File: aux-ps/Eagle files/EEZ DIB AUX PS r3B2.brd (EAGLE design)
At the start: 230.5 x 60 mm, 86 parts, among them IC2 MAX31760AEE+, IC3 BD00FC0WFP, J1 PF0030/PC, J2 4907, J3 4907, J4 4907, J5 SWEB 8094 AU/GN, Q1 BTA26-600, Q2 BTA26-600, Q3 2N7002, Q4 2N7002, Q5 2N7002, SW1 DF62J12S2AHQA, SW2 OS102011MA1QN1C, X1 39-28-1063, X2 39-30-1039, X3 ZL231-16PG, X4 47053-1000, X5 47053-1000

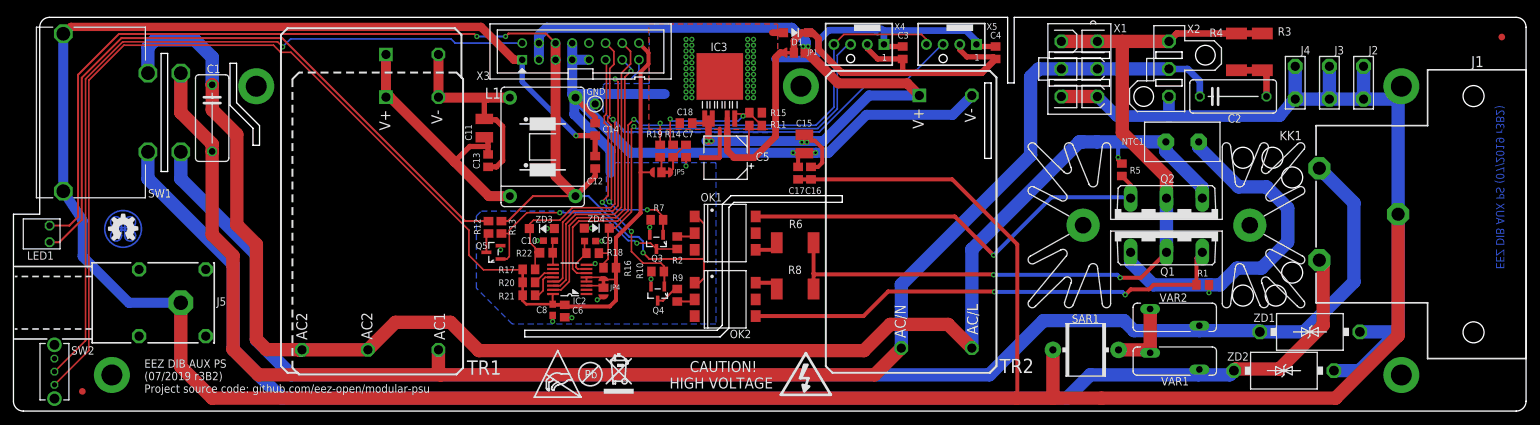
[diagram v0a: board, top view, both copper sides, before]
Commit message: AUX-PS PCB redesign
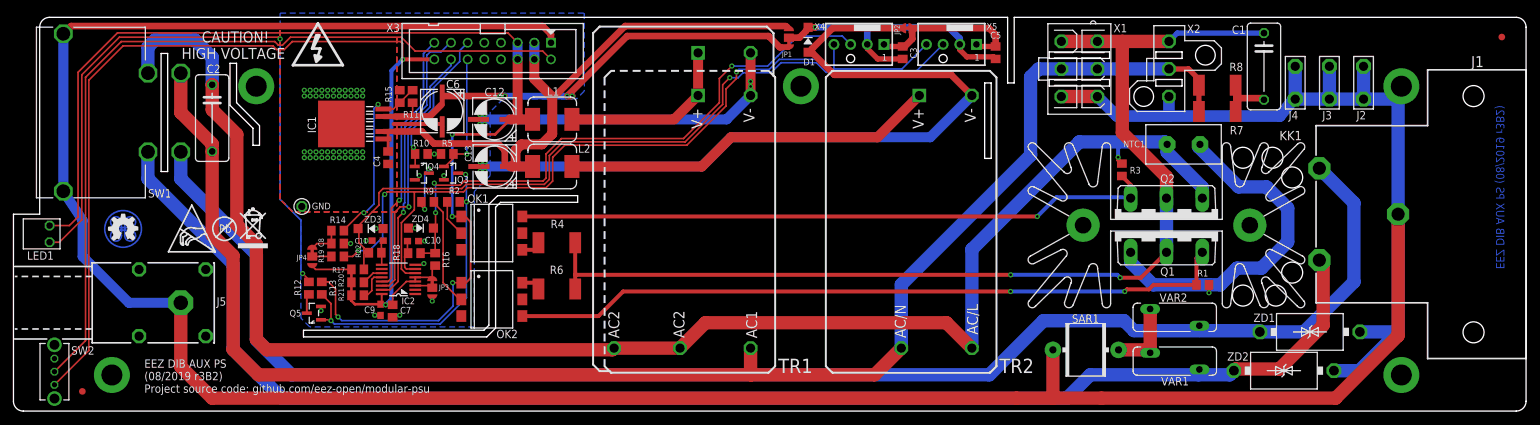
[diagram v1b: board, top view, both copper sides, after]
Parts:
- removed C14, C16, C17: (no value), rcl:C0805
- removed C15: 4u7, rcl:C1210
- removed C18: N.C., rcl:C0805
- removed IC3: BD00FC0WFP, EEZ_DIB:KVU5
- removed JP5: JP3-CUT, EEZ_Lib1:JP3-CUT
- added IC1: BD00FC0WFP, EEZ_DIB:KVU5
- added JP2: JP2-NOCUT, EEZ_Lib1:JP2-NOCUT
- added L2: VLS6045AF-3R3N, EEZ_inductors_and_transformers:COILCRAFT_HPI0630
- C11: value 4u7 -> 100n; device rcl:C1210 -> rcl:C0603
- C12, C13: value (none) -> EEEFK1V470P; device rcl:C0805 -> EEZ_Lib1:CAPAE660X610N
- C4: value 1u -> N.C.
- C5: value EEEFK1V470P -> 1u; device EEZ_Lib1:CAPAE660X610N -> rcl:C0805
- C6: value 1u -> EEEFK1V470P; device rcl:C0805 -> EEZ_Lib1:CAPAE660X610N
- C8: value 100n -> 1u; device rcl:C0603 -> rcl:C0805
- JP3: value JP2-NOCUT -> JP3-CUT; device EEZ_Lib1:JP2-NOCUT -> EEZ_Lib1:JP3-CUT
- L1: value (none) -> VLS6045AF-3R3N; device EEZ_inductors_and_transformers:RN212 -> EEZ_inductors_and_transformers:COILCRAFT_HPI0630
- R3: value 330R/2W -> 2K2; device rcl:R2512 -> rcl:R0805
- R5: value 2K2 -> 47K
- R7: value 47K -> 330R/2W; device rcl:R0805 -> rcl:R2512
- X3: value ZL231-16PG -> DS1013-16SSIB1
- moved C1 160.5 mm to (190.6, 52.5)
- moved C2 155.6 mm to (30.3, 44.6), turned to 270 degrees
- moved R4 107.6 mm to (82.8, 25.7), turned to 0 degrees
- moved R5 102.8 mm to (66.1, 39.2), turned to 0 degrees
- moved C4 94.0 mm to (57.1, 38.6), turned to 270 degrees
- moved R7 87.0 mm to (183.5, 45.7)
- moved JP3 78.7 mm to (63.8, 18.8), flipped to the top, turned to 270 degrees
- moved R8 71.4 mm to (183.5, 49.7)
- moved U$2 60.0 mm to (32.2, 27.8)
- moved U$3 60.0 mm to (34.2, 24.8)
- moved U$4 60.0 mm to (23.6, 24.3)
- moved R15 54.3 mm to (58.9, 47.9), turned to 90 degrees
- moved R14 52.5 mm to (49.4, 27.5), turned to 180 degrees
- moved R11 52.4 mm to (60.8, 47.9), turned to 90 degrees
- moved R19 51.7 mm to (49.4, 23.6), turned to 0 degrees
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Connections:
- removed net N$27: C11.1, C13.2, L1.1, TR1.V+, TR1.V+1
- removed net N$28: C11.2, C13.1, L1.3, TR1.V-, TR1.V-1
- new net N$15: L1.1, TR1.V+, TR1.V+1
- new net N$8: L2.1, TR2.V+
- net +12V: now also C13.1, C4.1, IC1.1, IC1.2, L2.2; no longer C15.1, C16.2, C18.1, IC3.1, IC3.2, TR2.V+
- net +3V3: now also C7.2, C9.2, JP3.NC, JP4.NO; no longer C6.2, C8.2, JP4.NC, JP5.NO
- net +5V: now also C12.1; no longer C12.2
- net 12V_PWM: now also C6.1, IC1.4; no longer C5.1, IC3.4
- net AC_L_OUT: now also C2.1, R3.2; no longer C1.1, R5.2
- net AC_N_OUT: now also C2.2, R7.1, R8.1; no longer C1.2, C2.1
- net AC_OUT_L: now also C1.1, R4.2; no longer R3.1, R4.1, R8.2
- net FAN_OUT+: now also C5.1; no longer C4.1
- net FAN_OUT-: now also C5.2, JP2.2; no longer C4.2, JP3.2
- net GND: now also C11.2, C12.2, C13.2, C4.2, C6.2, C7.1, C8.2, C9.1, IC1.3, JP2.1, JP3.NO, R5.1, TR1.V-, TR1.V-1; no longer C14.1, C15.2, C17.1, C18.2, C5.2, C6.1, C7.2, C8.1, C9.2, IC3.3, JP3.1, JP4.NO, L1.4, R7.1
- net N$11: now also IC1.5; no longer IC3.5
- net N$2: now also C10.1; no longer C9.1
- net N$21: now also C11.1; no longer C10.1
- net N$23: now also JP3.COM; no longer JP4.COM
- net N$4: now also JP4.COM; no longer JP5.COM
- net N$71: now also R3.1; no longer R5.1
- net N$73: now also R6.1; no longer R8.1
- net N$76: now also R4.1; no longer R6.1
- net N$83: now also C1.2, R7.2, R8.2; no longer C2.2, R3.2, R4.2
- net N$9: now also C8.1, JP4.NC; no longer C7.1, JP5.NC
- net PE: no longer C12.1, C14.2, C16.1, C17.2
- net PWR_DIRECT: now also R5.2; no longer R7.2
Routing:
- net PE: track 561.8 -> 484.2 mm, vias 3 -> 2
- net N$8: track 0.00 -> 57.4 mm
- net N$27: track 40.8 -> 0.00 mm
- net 12V_PWM: track 33.5 -> 73.0 mm, vias 0 -> 4
- net AC_OUT_L: track 128.7 -> 165.3 mm
- net PWM_OUT: track 93.5 -> 129.9 mm, vias 2 -> 3
- net GND: track 160.9 -> 196.2 mm, vias 58 -> 67
- net N$72: track 74.9 -> 110.0 mm
- net N$28: track 32.0 -> 0.00 mm
- net N$71: track 67.3 -> 98.0 mm
- net +12V: track 124.0 -> 95.0 mm, vias 6 -> 0
- net +3V3: track 204.7 -> 177.1 mm, vias 0 -> 2
- net N$15: track 0.00 -> 27.2 mm
- net FAN_SENSE1: track 68.7 -> 91.7 mm, vias 1 -> 3
- net FAN_SENSE2: track 92.0 -> 114.6 mm
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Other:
- outline, holes or cut-outs redrawn
- board text added: "EEZ DIB AUX PS (08/2019 r3B2)"
- board text added: "EEZ DIB AUX PS (08/2019 r3B2) Project source code: github.com/eez-open/modular-psu"
- board text removed: "EEZ DIB AUX PS (07/2019 r3B2)"
- board text removed: "EEZ DIB AUX PS (07/2019 r3B2) Project source code: github.com/eez-open/modular-psu"

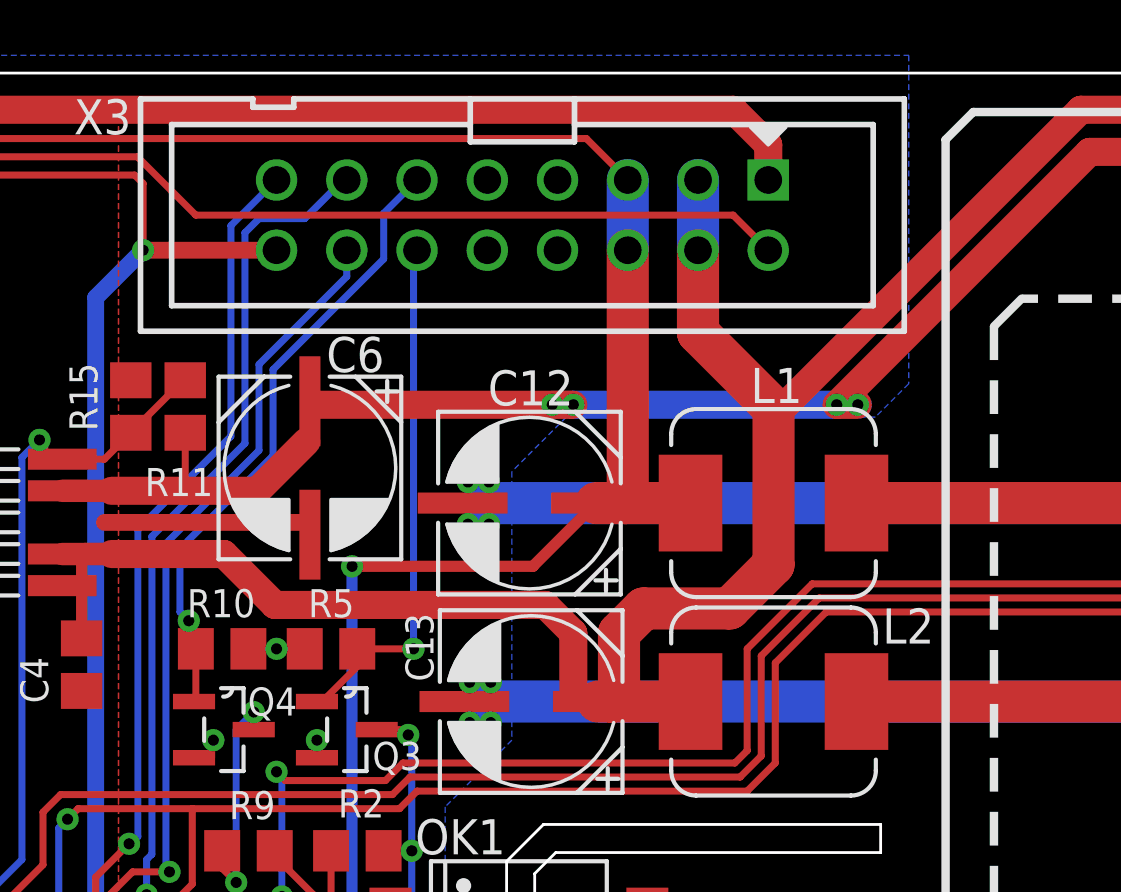
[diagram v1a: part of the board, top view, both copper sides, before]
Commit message: PCB test tabs added
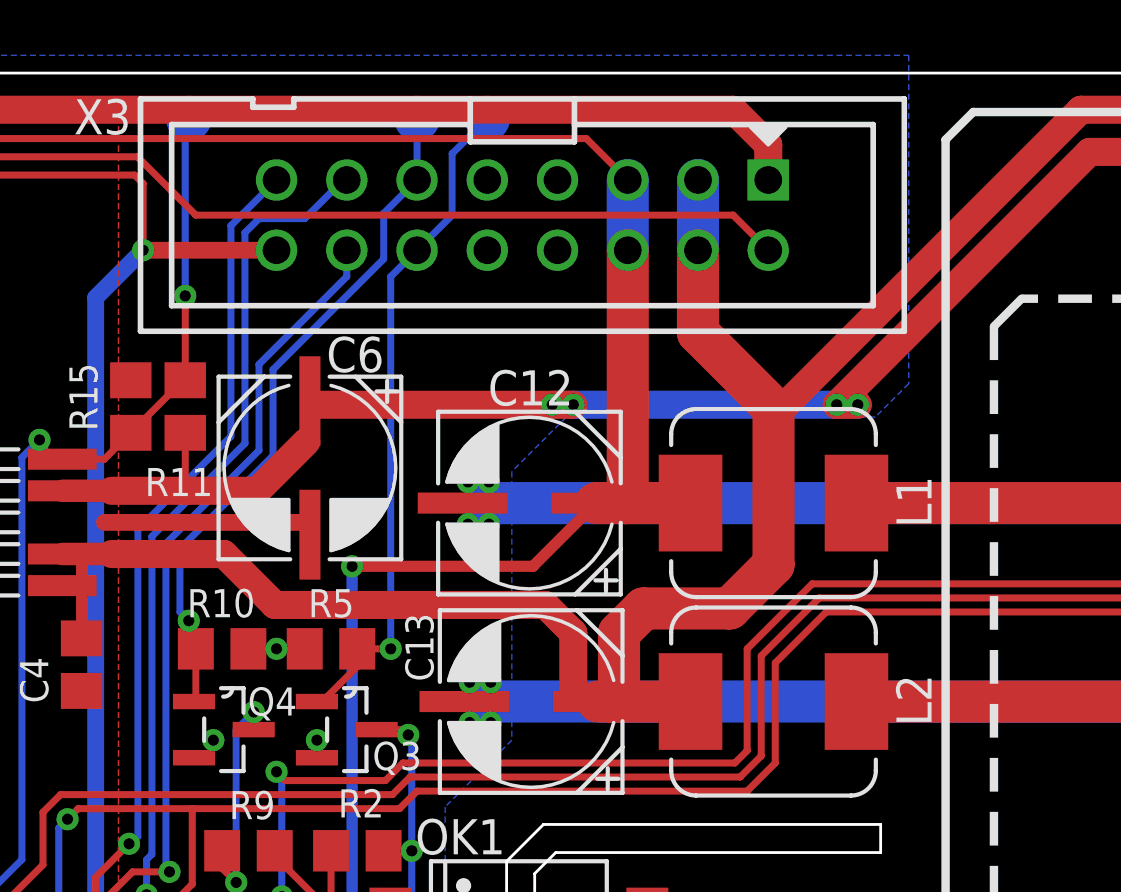
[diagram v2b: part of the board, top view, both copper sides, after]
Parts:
- added DIR, FB, SS: (no value), EEZ_Lib1:PCB_TEST_PAD
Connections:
- removed net N$11: IC1.5, R11.2, R14.1, R15.1
- new net LDO_FB: FB.NC, IC1.5, R11.2, R14.1, R15.1
- net PWR_DIRECT: now also DIR.NC
- net PWR_SSTART: now also SS.NC
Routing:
- net LDO_FB: track 0.00 -> 38.6 mm, vias 0 -> 3
- net N$11: track 29.1 -> 0.00 mm, vias 2 -> 0
- net PWR_DIRECT: track 19.3 -> 24.5 mm
- net PWR_SSTART: track 23.4 -> 25.7 mm
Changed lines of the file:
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@@
 <grid distance="2.5" unitdist="mil" unit="mil" style="lines" multiple="40" display="no" altdistance="12.5" altunitdist="mil" altunit="mil"/>
 <layers>
-<layer number="1" name="Top" color="11" fill="1" visible="no" active="yes"/>
+<layer number="1" name="Top" color="11" fill="1" visible="yes" active="yes"/>
 <layer number="2" name="Route2" color="1" fill="3" visible="no" active="no"/>
 <layer number="3" name="Route3" color="4" fill="3" visible="no" active="no"/>
@@
 <layer number="14" name="Route14" color="1" fill="6" visible="no" active="no"/>
 <layer number="15" name="Route15" color="4" fill="6" visible="no" active="no"/>
-<layer number="16" name="Bottom" color="1" fill="1" visible="no" active="yes"/>
-<layer number="17" name="Pads" color="6" fill="1" visible="no" active="yes"/>
-<layer number="18" name="Vias" color="6" fill="1" visible="no" active="yes"/>
-<layer number="19" name="Unrouted" color="6" fill="1" visible="no" active="yes"/>
+<layer number="16" name="Bottom" color="1" fill="1" visible="yes" active="yes"/>
+<layer number="17" name="Pads" color="6" fill="1" visible="yes" active="yes"/>
+<layer number="18" name="Vias" color="6" fill="1" visible="yes" active="yes"/>
+<layer number="19" name="Unrouted" color="6" fill="1" visible="yes" active="yes"/>
 <layer number="20" name="Dimension" color="12" fill="1" visible="yes" active="yes"/>
 <layer number="21" name="tPlace" color="7" fill="1" visible="yes" active="yes"/>
-<layer number="22" name="bPlace" color="13" fill="1" visible="no" active="yes"/>
+<layer number="22" name="bPlace" color="13" fill="1" visible="yes" active="yes"/>
 <layer number="23" name="tOrigins" color="15" fill="1" visible="yes" active="yes"/>
-<layer number="24" name="bOrigins" color="15" fill="1" visible="no" active="yes"/>
+<layer number="24" name="bOrigins" color="15" fill="1" visible="yes" active="yes"/>
 <layer number="25" name="tNames" color="7" fill="1" visible="yes" active="yes"/>
-<layer number="26" name="bNames" color="13" fill="1" visible="no" active="yes"/>
-<layer number="27" name="tValues" color="14" fill="1" visible="yes" active="yes"/>
-<layer number="28" name="bValues" color="11" fill="1" visible="no" active="yes"/>
-<layer number="29" name="tStop" color="15" fill="1" visible="yes" active="yes"/>
-<layer number="30" name="bStop" color="7" fill="1" visible="no" active="yes"/>
+<layer number="26" name="bNames" color="13" fill="1" visible="yes" active="yes"/>
+<layer number="27" name="tValues" color="14" fill="1" visible="no" active="yes"/>
+<layer number="28" name="bValues" color="11" fill="1" visible="yes" active="yes"/>
+<layer number="29" name="tStop" color="15" fill="1" visible="no" active="yes"/>
+<layer number="30" name="bStop" color="7" fill="1" visible="yes" active="yes"/>
 <layer number="31" name="tCream" color="7" fill="4" visible="no" active="yes"/>
 <layer number="32" name="bCream" color="7" fill="5" visible="no" active="yes"/>
@@
 <layer number="37" name="tTest" color="7" fill="1" visible="no" active="yes"/>
 <layer number="38" name="bTest" color="7" fill="1" visible="no" active="yes"/>
-<layer number="39" name="tKeepout" color="15" fill="1" visible="yes" active="yes"/>
+<layer number="39" name="tKeepout" color="15" fill="1" visible="no" active="yes"/>
 <layer number="40" name="bKeepout" color="13" fill="1" visible="no" active="yes"/>
 <layer number="41" name="tRestrict" color="4" fill="10" visible="no" active="yes"/>
@@
 <layer number="111" name="111" color="7" fill="1" visible="no" active="no"/>
 <layer number="112" name="tSilk" color="7" fill="1" visible="no" active="no"/>
+<layer number="114" name="EEZ" color="7" fill="1" visible="no" active="yes"/>
 <layer number="116" name="Patch_BOT" color="7" fill="1" visible="no" active="no"/>
 <layer number="118" name="Rect_Pads" color="7" fill="1" visible="no" active="no"/>
@@
 </element>
 <element name="L1" library="EEZ_inductors_and_transformers" package="COILCRAFT_HPI0630" value="VLS6045AF-3R3N" x="82.1055" y="44.45" smashed="yes" rot="R180">
-<attribute name="NAME" x="81.28" y="48.0695" size="1.27" layer="25" ratio="10"/>
+<attribute name="NAME" x="87.8205" y="43.561" size="1.27" layer="25" ratio="10" rot="R90"/>
 <attribute name="VALUE" x="82.1055" y="44.45" size="1.016" layer="27" ratio="10" rot="R180" align="center"/>
 </element>
 <element name="L2" library="EEZ_inductors_and_transformers" package="COILCRAFT_HPI0630" value="VLS6045AF-3R3N" x="82.1055" y="37.2745" smashed="yes" rot="R180">
-<attribute name="NAME" x="86.0425" y="39.37" size="1.27" layer="25" ratio="10"/>
+<attribute name="NAME" x="87.8205" y="36.3855" size="1.27" layer="25" ratio="10" rot="R90"/>
 <attribute name="VALUE" x="82.1055" y="37.2745" size="1.016" layer="27" ratio="10" rot="R180" align="center"/>
 </element>
@@
 <attribute name="VALUE" x="77.343" y="37.7317" size="0.8128" layer="27" ratio="10" rot="SR180"/>
 </element>
+<element name="DIR" library="EEZ_Lib1" package="PCB_TEST_PAD" value="" x="71.755" y="58.3565" smashed="yes" rot="MR0">
+<attribute name="NAME" x="74.676" y="57.9755" size="0.8128" layer="26" ratio="10" rot="MR0"/>
+</element>
+<element name="SS" library="EEZ_Lib1" package="PCB_TEST_PAD" value="" x="69.215" y="58.3565" smashed="yes" rot="MR0">
+<attribute name="NAME" x="68.072" y="58.039" size="0.8128" layer="26" ratio="10" rot="MR0"/>
+</element>
+<element name="FB" library="EEZ_Lib1" package="PCB_TEST_PAD" value="" x="60.96" y="58.3565" smashed="yes" rot="MR0">
+<attribute name="NAME" x="59.944" y="57.9755" size="0.8128" layer="26" ratio="10" rot="MR0"/>
+</element>
 </elements>
 <signals>
@@
 <contactref element="Q3" pad="1"/>
 <contactref element="R5" pad="2"/>
-<via x="69.088" y="39.1795" extent="1-16" drill="0.4" shape="octagon"/>
+<via x="68.2625" y="39.1795" extent="1-16" drill="0.4" shape="octagon"/>
 <wire x1="65.532" y1="37.338" x2="65.5955" y2="37.2745" width="0.254" layer="1"/>
-<wire x1="69.215" y1="53.594" x2="69.088" y2="53.594" width="0.254" layer="16"/>
-<wire x1="69.088" y1="53.594" x2="69.088" y2="39.1795" width="0.254" layer="16"/>
-<wire x1="67.0535" y1="39.1795" x2="69.088" y2="39.1795" width="0.254" layer="1"/>
+<wire x1="68.2625" y1="52.6415" x2="68.2625" y2="39.1795" width="0.254" layer="16"/>
+<wire x1="67.0535" y1="39.1795" x2="68.2625" y2="39.1795" width="0.254" layer="1"/>
 <wire x1="65.5955" y1="37.2745" x2="65.786" y2="37.2745" width="0.254" layer="1"/>
 <wire x1="65.786" y1="37.2745" x2="67.056" y2="38.5445" width="0.254" layer="1"/>
 <wire x1="67.056" y1="38.5445" x2="67.056" y2="39.177" width="0.254" layer="1"/>
 <wire x1="67.056" y1="39.177" x2="67.0535" y2="39.1795" width="0.254" layer="1"/>
+<contactref element="DIR" pad="NC"/>
+<wire x1="69.215" y1="53.594" x2="70.485" y2="54.864" width="0.254" layer="16"/>
+<wire x1="70.485" y1="54.864" x2="70.485" y2="57.0865" width="0.254" layer="16"/>
+<wire x1="70.485" y1="57.0865" x2="71.755" y2="58.3565" width="0.254" layer="16"/>
+<wire x1="68.2625" y1="52.6415" x2="69.215" y2="53.594" width="0.254" layer="16"/>
 </signal>
 <signal name="PWR_SSTART">
@@
 <wire x1="60.96" y1="40.1955" x2="60.96" y2="39.436" width="0.254" layer="1"/>
 <wire x1="60.96" y1="39.436" x2="61.2165" y2="39.1795" width="0.254" layer="1"/>
+<contactref element="SS" pad="NC"/>
+<wire x1="69.215" y1="56.134" x2="69.215" y2="58.3565" width="0.254" layer="16"/>
 </signal>
 <signal name="N$1">
@@
 <wire x1="60.833" y1="44.958" x2="60.8965" y2="44.8945" width="0.254" layer="1"/>
 </signal>
-<signal name="N$11">
+<signal name="LDO_FB">
 <contactref element="R15" pad="1"/>
 <contactref element="R11" pad="2"/>
@@
 <wire x1="55.753" y1="46.0375" x2="55.753" y2="46.5455" width="0.254" layer="1"/>
 <wire x1="55.753" y1="46.5455" x2="55.5625" y2="46.736" width="0.254" layer="1"/>
+<contactref element="FB" pad="NC"/>
+<wire x1="60.833" y1="48.8925" x2="60.833" y2="51.943" width="0.254" layer="1"/>
+<via x="60.833" y="51.943" extent="1-16" drill="0.4" shape="octagon"/>
+<wire x1="60.833" y1="51.943" x2="60.833" y2="58.166" width="0.254" layer="16"/>
+<wire x1="60.833" y1="58.166" x2="60.96" y2="58.3565" width="0.254" layer="16"/>
 </signal>
 <signal name="N$9">
